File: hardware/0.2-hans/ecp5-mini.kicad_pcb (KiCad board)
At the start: 4 copper layers, 52 x 27 mm, 81 parts, among them J2 JTAG, J3 S7 Mini, J4 S7 Mini, J5 USB_Type_C_2.0, Q500 BSS138, SW1 PTS810, U1 W25Q128JVPIQ, U2 ECP5U_12_CABGA256, U3 LP5907MFX-3.3, U4 LP5907MFX-2.5, U5 LP5907MFX-1.2, X1 16MHz

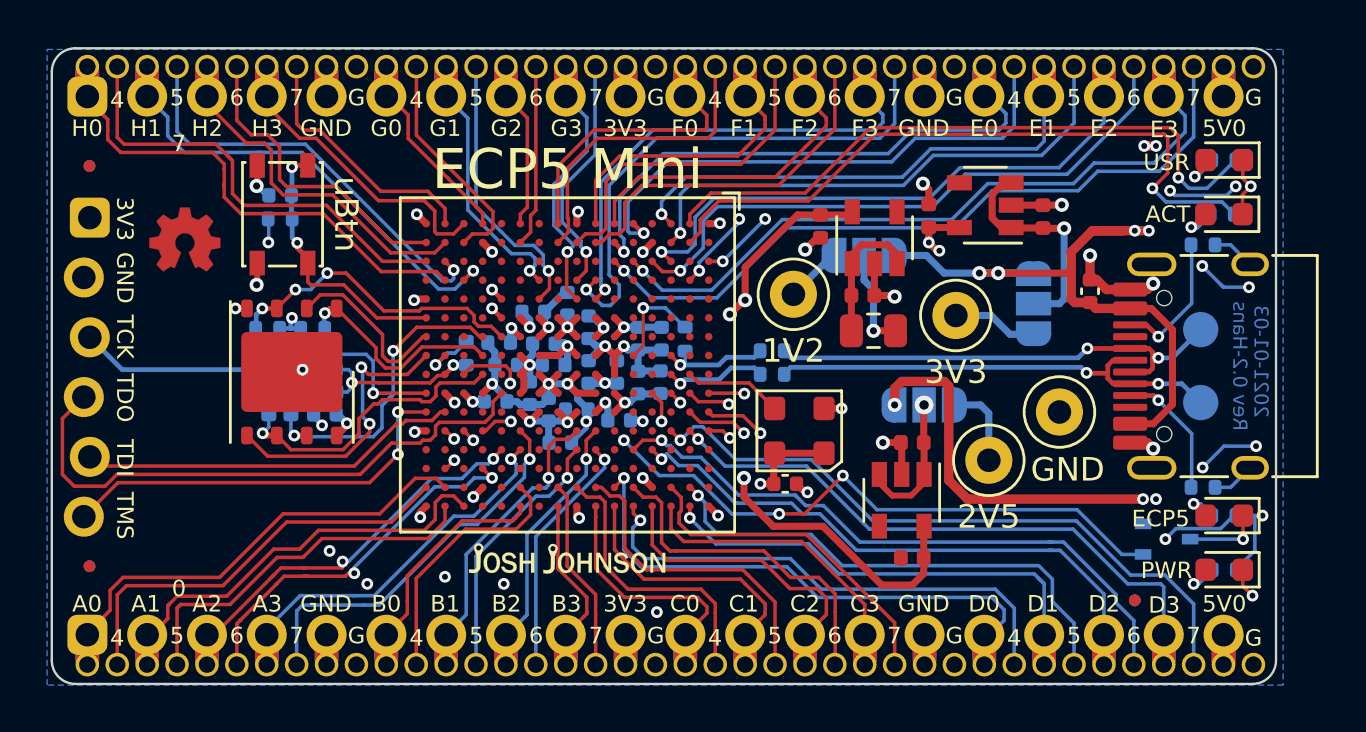
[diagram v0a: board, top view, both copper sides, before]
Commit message: remove usb, add 5v
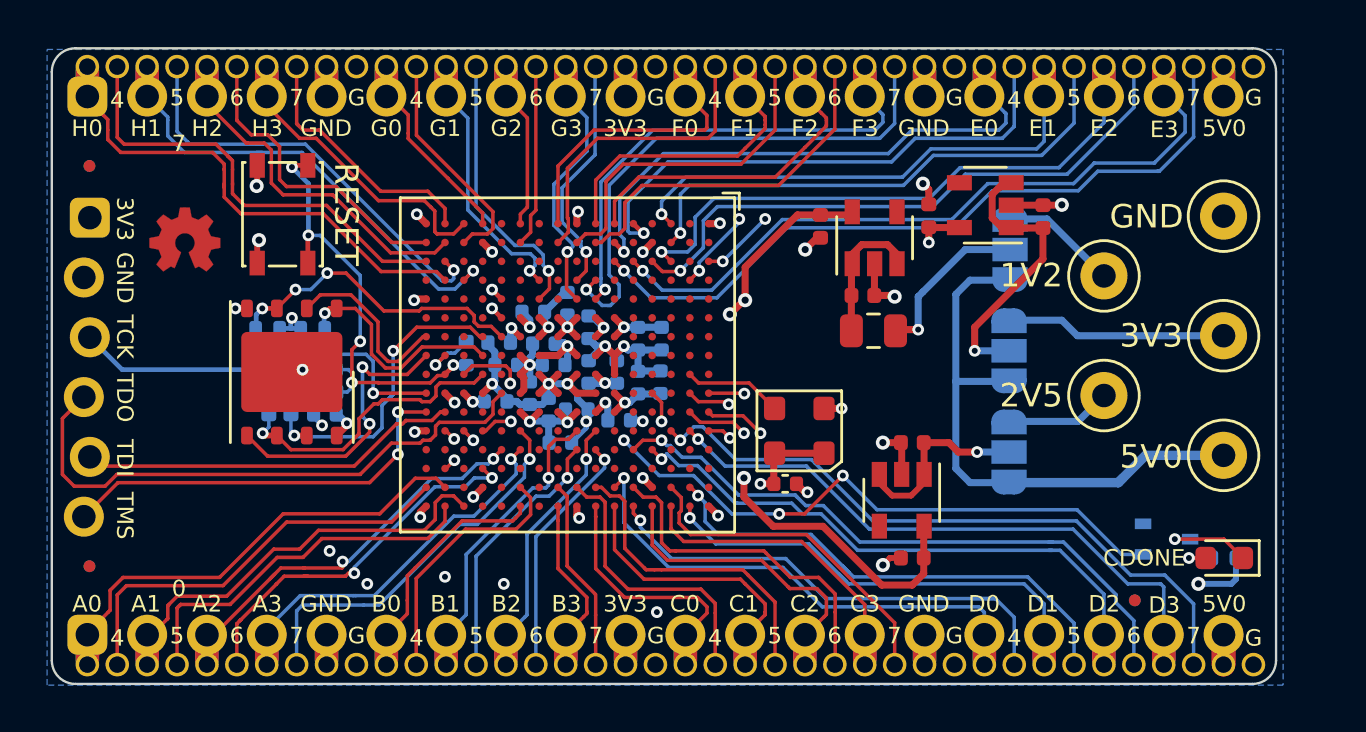
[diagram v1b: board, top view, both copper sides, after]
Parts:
- removed C16: 4u7, Capacitor_SMD:C_0402_1005Metric
- removed C523: 100n, Capacitor_SMD:C_0402_1005Metric
- removed D10, D12, D9: Pink, LED_SMD:LED_0603_1608Metric
- removed J5: USB_Type_C_2.0, josh-connectors:USB_C_Receptacle_HRO_TYPE-C-31-M-12
- removed LOGO1: Josh-Logo, josh-logos:josh-johnson-logo-8_6x1_5
- removed R500, R502, R503, R508: 1K5, Resistor_SMD:R_0402_1005Metric
- removed R504, R505, R516: 5K1, Resistor_SMD:R_0402_1005Metric
- removed R506, R507: 22R, Resistor_SMD:R_0402_1005Metric
- removed TP500: D+, TestPoint:TestPoint_Pad_D1.5mm
- removed TP501: D-, TestPoint:TestPoint_Pad_D1.5mm
- added TP5: 5V0, josh-test-point:Test-Point-Loop-RED, F.Cu at (146.0, 98.7)
- U2: value ECP5U_12_CABGA256 -> ECP5U_25_CABGA256
- moved TP1 13.2 mm to (140.9, 91.1)
- moved TP2 11.4 mm to (146.0, 93.7)
- moved TP4 10.9 mm to (146.0, 88.6)
- moved JP1 6.21 mm to (136.9, 90.0), turned to -90 degrees
- moved TP3 5.61 mm to (140.9, 96.2)
- moved JP3 4.12 mm to (136.9, 98.6), turned to -90 degrees
- moved JP2 2.26 mm to (136.9, 94.3), turned to -90 degrees
- moved D11 1.80 mm to (146.0, 103.1)
- moved R501 1.80 mm to (146.0, 103.1)
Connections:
- SW1 pad 2: /FPGA Config/nBTN_USR -> /FPGA Config/nFPGA_RST
- U2 pad B1: /LED_USR -> (no net)
- U2 pad B2: /LED_ACT -> (no net)
- U2 pad C8: /USB_D+ -> (no net)
- U2 pad C9: /USB_D- -> (no net)
- U2 pad E8: /USB_PU -> (no net)
- U2 pad T6: /FPGA Config/nBTN_USR -> (no net)
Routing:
- net /LED_ACT: track 28.9 -> 0.00 mm, vias 1 -> 0
- net /LED_USR: track 27.7 -> 0.00 mm, vias 1 -> 0
- net +5V: track 79.4 -> 52.4 mm, vias 9 -> 0
- net /FPGA Config/D+: track 20.3 -> 0.00 mm, vias 2 -> 0
- net /FPGA Config/D-: track 20.0 -> 0.00 mm, vias 2 -> 0
- net +3V3: track 45.9 -> 30.8 mm, vias 21 -> 12
- net /FPGA Config/nFPGA_RST: track 7.29 -> 20.0 mm, vias 2 -> 5
- net GND: track 65.0 -> 52.6 mm, vias 44 -> 40
- net /FPGA Config/nBTN_USR: track 11.6 -> 0.00 mm, vias 2 -> 0
- net Net-(J5-PadB5): track 5.89 -> 0.00 mm, vias 1 -> 0
- net Net-(J5-PadA5): track 5.86 -> 0.00 mm, vias 1 -> 0
- net Net-(JP2-Pad1): track 3.63 -> 9.47 mm
- net /USB_D+: track 5.40 -> 0.00 mm, vias 1 -> 0
- net /USB_D-: track 4.37 -> 0.00 mm, vias 1 -> 0
- net /USB_PU: track 4.32 -> 0.00 mm, vias 1 -> 0
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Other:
- board text added: "CDONE"
- board text added: "RESET"
- board text removed: "2021-01-03"
- board text removed: "ACT"
- board text removed: "D+"
- board text removed: "D-"
- board text removed: "ECP5"
- board text removed: "ECP5 Mini"
- board text removed: "PWR"
- board text removed: "Rev 0.2-Hans"
- board text removed: "USB"
- board text removed: "USR"
- board text removed: "uBtn"
